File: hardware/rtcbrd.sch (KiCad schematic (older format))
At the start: 15 parts, among them J1 02x04, Q1 SI2302, Q2 AO3407, U1 PCF8563TS, Y1 32.768kHz

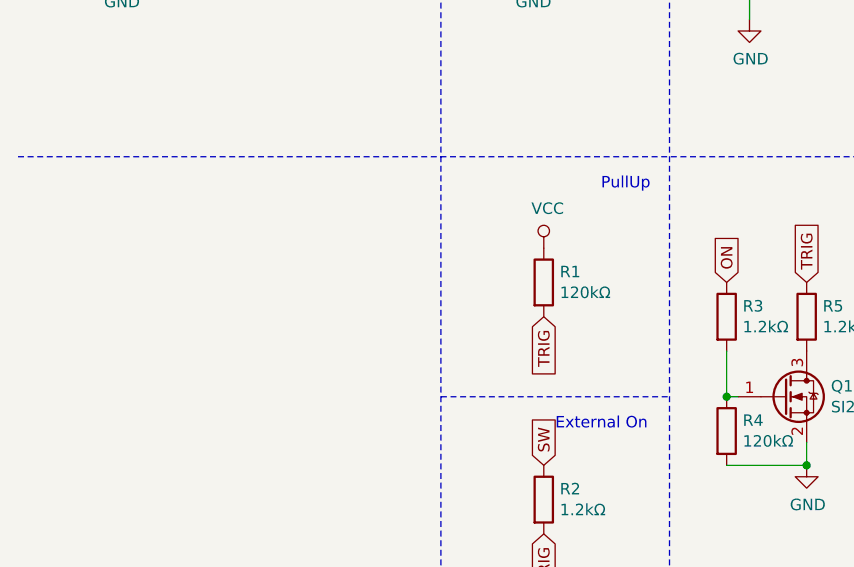
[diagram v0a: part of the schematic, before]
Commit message: Add I²C Pull-Up; Move value markings
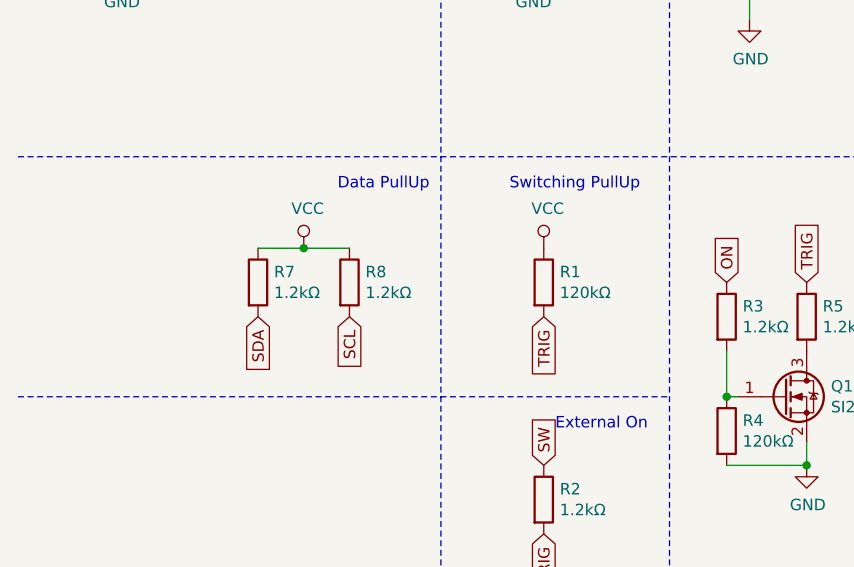
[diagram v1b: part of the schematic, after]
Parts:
- added R7, R8: 1.2kΩ, Resistors_SMD:R_0402, symbol Device:R
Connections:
- net SCL: now also R8.2
- net SDA: now also R7.2
- net VCC: now also R7.1, R8.1
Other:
- note added: "Data PullUp"
- note added: "Switching PullUp"
- note removed: "PullUp"
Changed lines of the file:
@@
-$EndComp
-$Comp
-L Device:R R1
-U 1 1 5D7B21B9
-P 2800 2900
-F 0 "R1" H 2870 2946 50  0000 L CNN
-F 1 "120kΩ" H 2870 2855 50  0000 L CNN
-F 2 "Resistors_SMD:R_0402" V 2730 2900 50  0001 C CNN
-F 3 "~" H 2800 2900 50  0001 C CNN
-	1    2800 2900
-	1    0    0    -1
 $EndComp
 $Comp
@@
 F 3 "" H 3950 3700 50  0001 C CNN
 	1    3950 3700
-	1    0    0    -1
-$EndComp
-$Comp
-L power:VCC #PWR0105
-U 1 1 5D7BA6A6
-P 2800 2750
-F 0 "#PWR0105" H 2800 2600 50  0001 C CNN
-F 1 "VCC" H 2817 2923 50  0000 C CNN
-F 2 "" H 2800 2750 50  0001 C CNN
-F 3 "" H 2800 2750 50  0001 C CNN
-	1    2800 2750
 	1    0    0    -1
 $EndComp
@@
 Text Notes 6100 600  0    50   ~ 0
 RTC
-Text GLabel 2800 3050 3    50   Input ~ 0
-TRIG
 Text GLabel 2800 4000 3    50   Input ~ 0
 TRIG
-Wire Notes Line
-	2350 3400 3350 3400
 Wire Notes Line
 	2350 500  2350 4350
@@
 Text Notes 4250 2500 0    50   ~ 0
 Digital On
-Text Notes 3050 2500 0    50   ~ 0
-PullUp
+Text Notes 2650 2500 0    50   ~ 0
+Switching PullUp
 Text Notes 2850 3550 0    50   ~ 0
 External On\n
@@
 Text GLabel 1450 1400 2    50   Input ~ 0
 SCL
+Text GLabel 2800 3050 3    50   Input ~ 0
+TRIG
+$Comp
+L power:VCC #PWR0105
+U 1 1 5D7BA6A6
+P 2800 2750
+F 0 "#PWR0105" H 2800 2600 50  0001 C CNN
+F 1 "VCC" H 2817 2923 50  0000 C CNN
+F 2 "" H 2800 2750 50  0001 C CNN
+F 3 "" H 2800 2750 50  0001 C CNN
+	1    2800 2750
+	1    0    0    -1
+$EndComp
+$Comp
+L Device:R R1
+U 1 1 5D7B21B9
+P 2800 2900
+F 0 "R1" H 2870 2946 50  0000 L CNN
+F 1 "120kΩ" H 2870 2855 50  0000 L CNN
+F 2 "Resistors_SMD:R_0402" V 2730 2900 50  0001 C CNN
+F 3 "~" H 2800 2900 50  0001 C CNN
+	1    2800 2900
+	1    0    0    -1
+$EndComp
+$Comp
+L power:VCC #PWR0115
+U 1 1 5E55A4F4
+P 1750 2750
+F 0 "#PWR0115" H 1750 2600 50  0001 C CNN
+F 1 "VCC" H 1767 2923 50  0000 C CNN
+F 2 "" H 1750 2750 50  0001 C CNN
+F 3 "" H 1750 2750 50  0001 C CNN
+	1    1750 2750
+	1    0    0    -1
+$EndComp
+$Comp
+L Device:R R8
+U 1 1 5E55A4FA
+P 1950 2900
+F 0 "R8" H 2020 2946 50  0000 L CNN
+F 1 "1.2kΩ" H 2020 2855 50  0000 L CNN
+F 2 "Resistors_SMD:R_0402" V 1880 2900 50  0001 C CNN
+F 3 "~" H 1950 2900 50  0001 C CNN
+	1    1950 2900
+	1    0    0    -1
+$EndComp
+$Comp
+L Device:R R7
+U 1 1 5E55B16D
+P 1550 2900
+F 0 "R7" H 1620 2946 50  0000 L CNN
+F 1 "1.2kΩ" H 1620 2855 50  0000 L CNN
+F 2 "Resistors_SMD:R_0402" V 1480 2900 50  0001 C CNN
+F 3 "~" H 1550 2900 50  0001 C CNN
+	1    1550 2900
+	1    0    0    -1
+$EndComp
+Text GLabel 1550 3050 3    50   Input ~ 0
+SDA
+Text GLabel 1950 3050 3    50   Input ~ 0
+SCL
+Wire Wire Line
+	1550 2750 1750 2750
+Wire Wire Line
+	1750 2750 1950 2750
+Connection ~ 1750 2750
+Text Notes 2300 2500 2    50   ~ 0
+Data PullUp
+Wire Notes Line
+	500  3400 3350 3400
 $EndSCHEMATC
